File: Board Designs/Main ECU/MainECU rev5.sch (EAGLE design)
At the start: 164 parts, among them Q10 MMBT3904LT3G, Q11 MMBT3904LT3G, Q9 MMBT3904LT3G, X1 CONNECTOR-37, X2 CONNECTOR-4AUTOSPORT, X3 CONNECTOR-4NANO-FIT-VERTICAL-4, X4 CONNECTOR-4NANO-FIT-VERTICAL-4

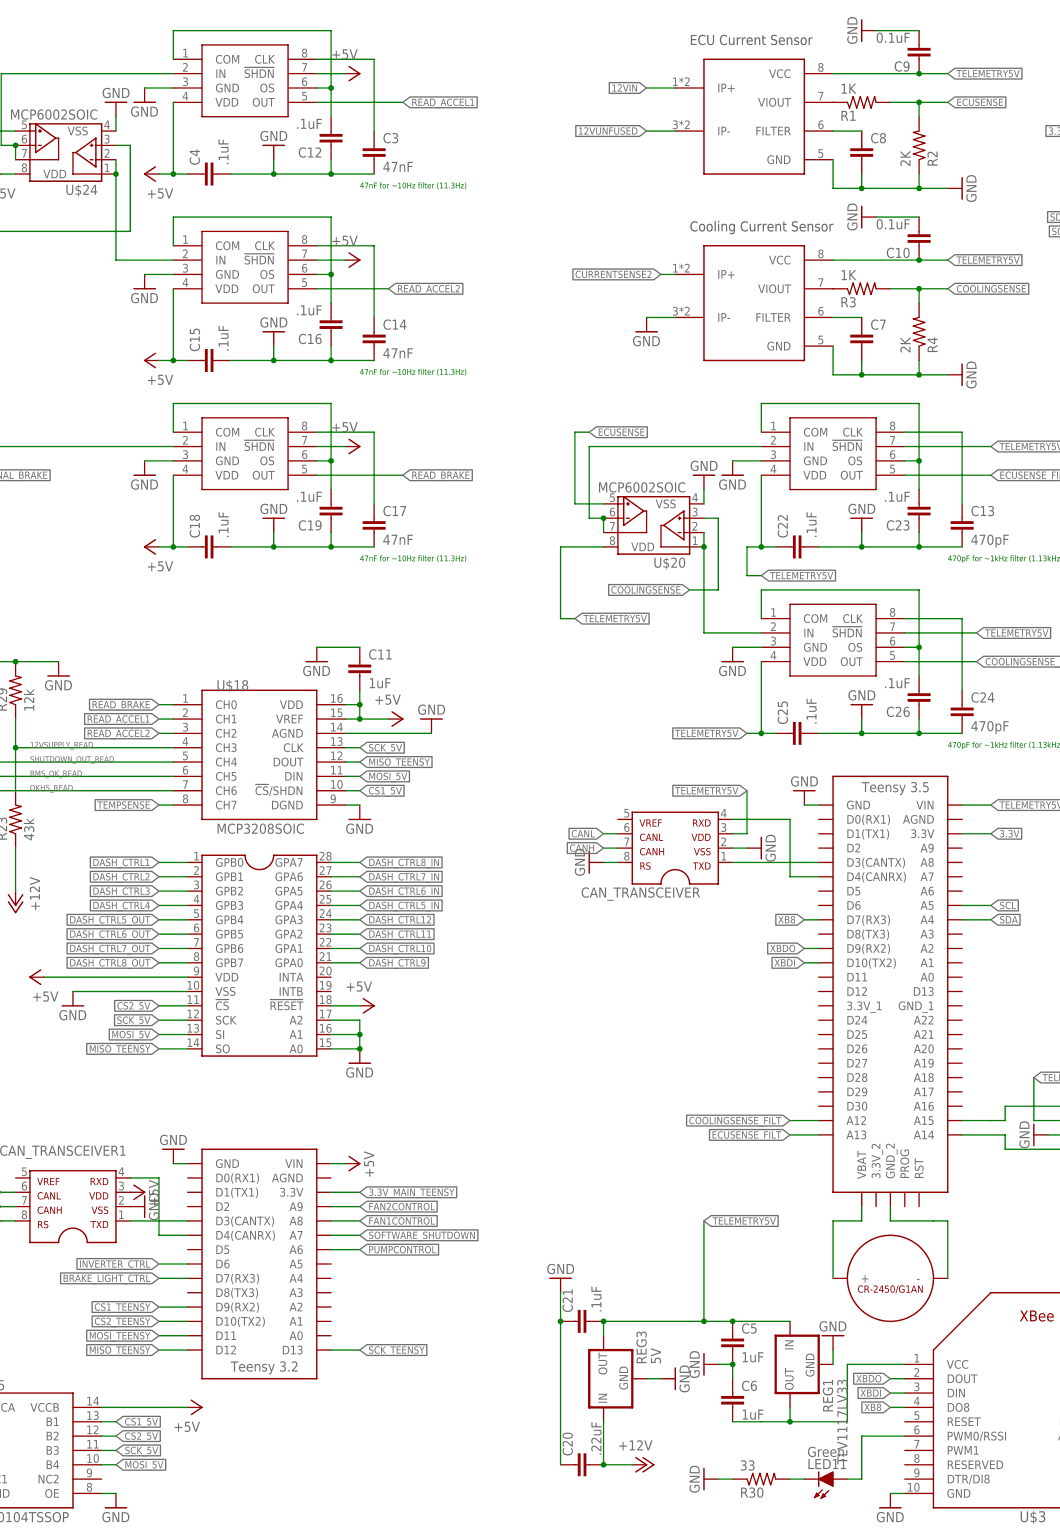
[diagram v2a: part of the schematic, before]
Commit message: MainECU rev5: Added current sensor filter caps, fixed level shifter OE pin, various tweaks to traces
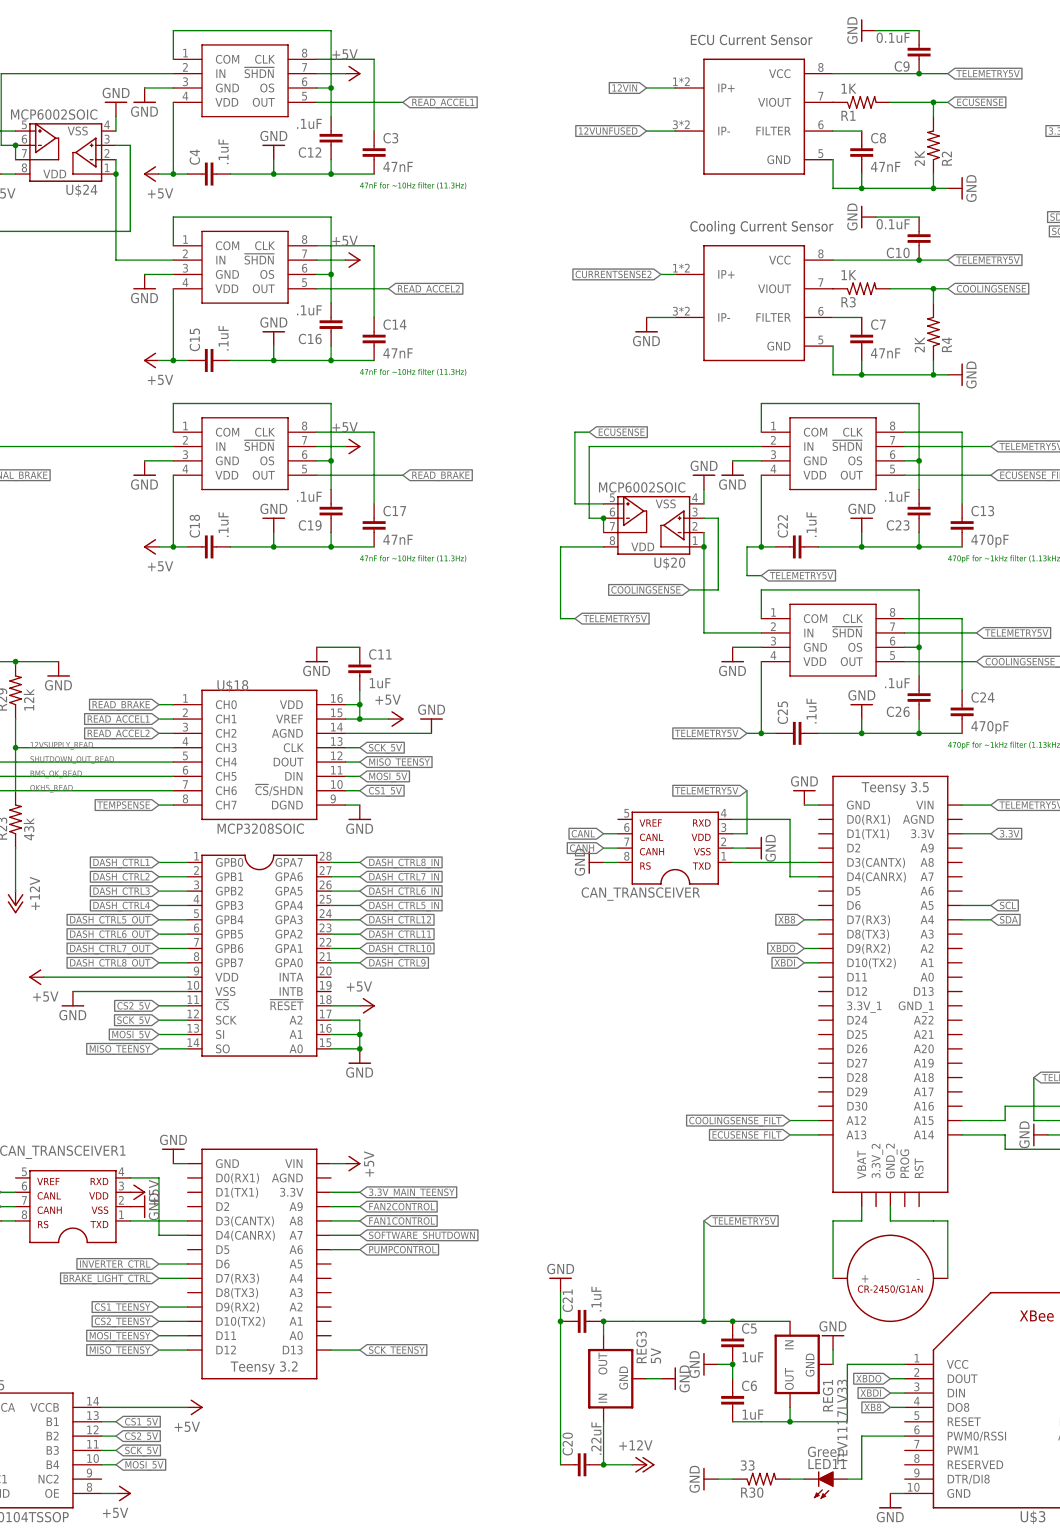
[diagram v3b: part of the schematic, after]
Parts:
- C7, C8: value (none) -> 47nF
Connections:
- net +5V: now also U$25.OE
- net GND: no longer U$25.OE
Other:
- moved on the sheet: R2, R4
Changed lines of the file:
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@@
 <part name="GND25" library="HyTechSymbols" deviceset="GND" device=""/>
 <part name="GND41" library="HyTechSymbols" deviceset="GND" device=""/>
-<part name="C7" library="HyTechDevices" deviceset="CAP" device="0805"/>
-<part name="C8" library="HyTechDevices" deviceset="CAP" device="0805"/>
+<part name="C7" library="HyTechDevices" deviceset="CAP" device="0805" value="47nF"/>
+<part name="C8" library="HyTechDevices" deviceset="CAP" device="0805" value="47nF"/>
 <part name="C9" library="HyTechDevices" deviceset="CAP" device="0805" value="0.1uF"/>
 <part name="C10" library="HyTechDevices" deviceset="CAP" device="0805" value="0.1uF"/>
@@
 <part name="R50" library="HyTechDevices" deviceset="RESISTOR" device="0805-RES" value="1k"/>
 <part name="FLIP" library="supply1" library_urn="urn:adsk.eagle:library:371" deviceset="+5V" device=""/>
-<part name="GND42" library="HyTechSymbols" deviceset="GND" device=""/>
 <part name="GND43" library="HyTechSymbols" deviceset="GND" device=""/>
 <part name="U$25" library="HyTechDevices" deviceset="TXB0104" device="TSSOP"/>
@@
 <part name="R52" library="HyTechDevices" deviceset="RESISTOR" device="0805-RES" value="100"/>
 <part name="GND79" library="HyTechSymbols" deviceset="GND" device=""/>
+<part name="FLIP1" library="supply1" library_urn="urn:adsk.eagle:library:371" deviceset="+5V" device=""/>
 </parts>
 <sheets>
@@
 <attribute name="VALUE" x="443.23" y="257.302" size="1.778" layer="96" rot="MR180"/>
 </instance>
-<instance part="R2" gate="G$1" x="457.2" y="246.38" smashed="yes" rot="MR90">
-<attribute name="NAME" x="458.6986" y="242.57" size="1.778" layer="95" rot="MR90"/>
-<attribute name="VALUE" x="453.898" y="242.57" size="1.778" layer="96" rot="MR90"/>
+<instance part="R2" gate="G$1" x="459.74" y="246.38" smashed="yes" rot="MR90">
+<attribute name="NAME" x="461.2386" y="242.57" size="1.778" layer="95" rot="MR90"/>
+<attribute name="VALUE" x="456.438" y="242.57" size="1.778" layer="96" rot="MR90"/>
 </instance>
 <instance part="R3" gate="G$1" x="447.04" y="220.98" smashed="yes" rot="MR180">
@@
 <attribute name="VALUE" x="443.23" y="224.282" size="1.778" layer="96" rot="MR180"/>
 </instance>
-<instance part="R4" gate="G$1" x="457.2" y="213.36" smashed="yes" rot="MR90">
-<attribute name="NAME" x="458.6986" y="209.55" size="1.778" layer="95" rot="MR90"/>
-<attribute name="VALUE" x="453.898" y="209.55" size="1.778" layer="96" rot="MR90"/>
+<instance part="R4" gate="G$1" x="459.74" y="213.36" smashed="yes" rot="MR90">
+<attribute name="NAME" x="461.2386" y="209.55" size="1.778" layer="95" rot="MR90"/>
+<attribute name="VALUE" x="456.438" y="209.55" size="1.778" layer="96" rot="MR90"/>
 </instance>
 <instance part="CAN_TRANSCEIVER" gate="G$1" x="421.64" y="127" smashed="yes" rot="R180">
@@
 <attribute name="VALUE" x="325.12" y="20.32" size="1.778" layer="96" rot="MR180"/>
 </instance>
-<instance part="GND42" gate="1" x="314.96" y="5.08" smashed="yes">
-<attribute name="VALUE" x="312.42" y="2.54" size="1.778" layer="96"/>
-</instance>
 <instance part="GND43" gate="1" x="281.94" y="5.08" smashed="yes">
 <attribute name="VALUE" x="279.4" y="2.54" size="1.778" layer="96"/>
@@
 <instance part="GND79" gate="1" x="584.2" y="137.16" smashed="yes">
 <attribute name="VALUE" x="581.66" y="134.62" size="1.778" layer="96"/>
+</instance>
+<instance part="FLIP1" gate="1" x="317.5" y="7.62" smashed="yes" rot="MR90">
+<attribute name="VALUE" x="312.42" y="5.08" size="1.778" layer="96" rot="MR180"/>
 </instance>
 </instances>
@@
 <segment>
 <pinref part="GND25" gate="1" pin="GND"/>
-<wire x1="462.28" y1="205.74" x2="457.2" y2="205.74" width="0.1524" layer="91"/>
+<wire x1="462.28" y1="205.74" x2="459.74" y2="205.74" width="0.1524" layer="91"/>
 <pinref part="U$10" gate="G$1" pin="GND"/>
-<wire x1="457.2" y1="205.74" x2="447.04" y2="205.74" width="0.1524" layer="91"/>
+<wire x1="459.74" y1="205.74" x2="447.04" y2="205.74" width="0.1524" layer="91"/>
 <wire x1="447.04" y1="205.74" x2="441.96" y2="205.74" width="0.1524" layer="91"/>
 <wire x1="441.96" y1="205.74" x2="441.96" y2="210.82" width="0.1524" layer="91"/>
@@
 <junction x="447.04" y="205.74"/>
 <pinref part="R4" gate="G$1" pin="1"/>
-<wire x1="457.2" y1="208.28" x2="457.2" y2="205.74" width="0.1524" layer="91"/>
-<junction x="457.2" y="205.74"/>
+<wire x1="459.74" y1="208.28" x2="459.74" y2="205.74" width="0.1524" layer="91"/>
+<junction x="459.74" y="205.74"/>
 </segment>
 <segment>
@@
 <segment>
 <pinref part="GND41" gate="1" pin="GND"/>
-<wire x1="462.28" y1="238.76" x2="457.2" y2="238.76" width="0.1524" layer="91"/>
+<wire x1="462.28" y1="238.76" x2="459.74" y2="238.76" width="0.1524" layer="91"/>
 <pinref part="U$9" gate="G$1" pin="GND"/>
-<wire x1="457.2" y1="238.76" x2="447.04" y2="238.76" width="0.1524" layer="91"/>
+<wire x1="459.74" y1="238.76" x2="447.04" y2="238.76" width="0.1524" layer="91"/>
 <wire x1="447.04" y1="238.76" x2="441.96" y2="238.76" width="0.1524" layer="91"/>
 <wire x1="441.96" y1="238.76" x2="441.96" y2="243.84" width="0.1524" layer="91"/>
@@
 <junction x="447.04" y="238.76"/>
 <pinref part="R2" gate="G$1" pin="1"/>
-<wire x1="457.2" y1="241.3" x2="457.2" y2="238.76" width="0.1524" layer="91"/>
-<junction x="457.2" y="238.76"/>
+<wire x1="459.74" y1="241.3" x2="459.74" y2="238.76" width="0.1524" layer="91"/>
+<junction x="459.74" y="238.76"/>
 </segment>
 <segment>
@@
 <pinref part="GND11" gate="1" pin="GND"/>
 <wire x1="203.2" y1="195.58" x2="203.2" y2="193.04" width="0.1524" layer="91"/>
-</segment>
-<segment>
-<wire x1="312.42" y1="7.62" x2="314.96" y2="7.62" width="0.1524" layer="91"/>
-<pinref part="GND42" gate="1" pin="GND"/>
-<pinref part="U$25" gate="G$1" pin="OE"/>
 </segment>
 <segment>
@@
 <pinref part="U$25" gate="G$1" pin="VCCB"/>
 </segment>
+<segment>
+<wire x1="312.42" y1="7.62" x2="314.96" y2="7.62" width="0.1524" layer="91"/>
+<pinref part="U$25" gate="G$1" pin="OE"/>
+<pinref part="FLIP1" gate="1" pin="+5V"/>
+</segment>
 </net>
 <net name="IMD_PWR_STEP" class="0">
@@
 <pinref part="R1" gate="G$1" pin="2"/>
 <pinref part="R2" gate="G$1" pin="2"/>
-<wire x1="452.12" y1="254" x2="457.2" y2="254" width="0.1524" layer="91"/>
+<wire x1="452.12" y1="254" x2="459.74" y2="254" width="0.1524" layer="91"/>
 <label x="462.28" y="254" size="1.27" layer="95" xref="yes"/>
-<wire x1="457.2" y1="254" x2="462.28" y2="254" width="0.1524" layer="91"/>
-<wire x1="457.2" y1="251.46" x2="457.2" y2="254" width="0.1524" layer="91"/>
-<junction x="457.2" y="254"/>
+<wire x1="459.74" y1="254" x2="462.28" y2="254" width="0.1524" layer="91"/>
+<wire x1="459.74" y1="251.46" x2="459.74" y2="254" width="0.1524" layer="91"/>
+<junction x="459.74" y="254"/>
 </segment>
 <segment>
@@
 <pinref part="R3" gate="G$1" pin="2"/>
 <pinref part="R4" gate="G$1" pin="2"/>
-<wire x1="452.12" y1="220.98" x2="457.2" y2="220.98" width="0.1524" layer="91"/>
-<wire x1="457.2" y1="220.98" x2="457.2" y2="218.44" width="0.1524" layer="91"/>
-<wire x1="457.2" y1="220.98" x2="462.28" y2="220.98" width="0.1524" layer="91"/>
-<junction x="457.2" y="220.98"/>
+<wire x1="452.12" y1="220.98" x2="459.74" y2="220.98" width="0.1524" layer="91"/>
+<wire x1="459.74" y1="220.98" x2="459.74" y2="218.44" width="0.1524" layer="91"/>
+<wire x1="459.74" y1="220.98" x2="462.28" y2="220.98" width="0.1524" layer="91"/>
+<junction x="459.74" y="220.98"/>
 <label x="462.28" y="220.98" size="1.27" layer="95" xref="yes"/>
 </segment>

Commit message: Main ECU rev{1-5}: Update values of LED resistors based on testing
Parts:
- LED7: value Green -> 20k
- R11: value 43 -> 150
- R14, R21: value 820 -> 2k
- R16, R25, R32, R51, R52: value 100 -> 1.2k
- R31: value 1.2K -> 6.8k
- R45: value 33 -> 0
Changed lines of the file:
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@@
 <part name="BMS_SSR" library="HyTechDevices" deviceset="CPC1002N" device=""/>
 <part name="GND3" library="HyTechSymbols" deviceset="GND" device=""/>
-<part name="R11" library="HyTechDevices" deviceset="RESISTOR" device="0805-RES" value="43"/>
+<part name="R11" library="HyTechDevices" deviceset="RESISTOR" device="0805-RES" value="150"/>
 <part name="R12" library="HyTechDevices" deviceset="RESISTOR" device="0805-RES" value="33"/>
 <part name="BMS_LATCH_SSR" library="HyTechDevices" deviceset="CPC1002N" device=""/>
@@
 <part name="LED3" library="HyTechDevices" deviceset="LED" device="-0805" value="Green"/>
 <part name="LED5" library="HyTechDevices" deviceset="LED" device="-0805" value="Yellow"/>
-<part name="R14" library="HyTechDevices" deviceset="RESISTOR" device="0805-RES" value="820"/>
+<part name="R14" library="HyTechDevices" deviceset="RESISTOR" device="0805-RES" value="2k"/>
 <part name="GND6" library="HyTechSymbols" deviceset="GND" device=""/>
 <part name="IMD_SHUTDOWN1" library="HyTechDevices" deviceset="G2RL-2-DC12" device=""/>
 <part name="GND19" library="HyTechSymbols" deviceset="GND" device=""/>
 <part name="R17" library="HyTechDevices" deviceset="RESISTOR" device="0805-RES" value="820"/>
-<part name="LED7" library="HyTechDevices" deviceset="LED" device="-0805" value="Green"/>
+<part name="LED7" library="HyTechDevices" deviceset="LED" device="-0805" value="20k"/>
 <part name="GND20" library="HyTechSymbols" deviceset="GND" device=""/>
 <part name="GND21" library="HyTechSymbols" deviceset="GND" device=""/>
@@
 <part name="LED9" library="HyTechDevices" deviceset="LED" device="-0805" value="Yellow"/>
 <part name="GND24" library="HyTechSymbols" deviceset="GND" device=""/>
-<part name="R21" library="HyTechDevices" deviceset="RESISTOR" device="0805-RES" value="820"/>
+<part name="R21" library="HyTechDevices" deviceset="RESISTOR" device="0805-RES" value="2k"/>
 <part name="P+10" library="supply1" deviceset="+12V" device=""/>
 <part name="P+5" library="supply1" deviceset="+12V" device=""/>
@@
 <part name="LED18" library="HyTechDevices" deviceset="LED" device="-0805" value="RED"/>
 <part name="GND45" library="HyTechSymbols" deviceset="GND" device=""/>
-<part name="R31" library="HyTechDevices" deviceset="RESISTOR" device="0805-RES" value="1.2K"/>
+<part name="R31" library="HyTechDevices" deviceset="RESISTOR" device="0805-RES" value="6.8k"/>
 <part name="GND1" library="HyTechSymbols" deviceset="GND" device=""/>
 <part name="GND4" library="HyTechSymbols" deviceset="GND" device=""/>
@@
 <part name="GND53" library="HyTechSymbols" deviceset="GND" device=""/>
 <part name="LED10" library="HyTechDevices" deviceset="LED" device="-0805" value="Red"/>
-<part name="R32" library="HyTechDevices" deviceset="RESISTOR" device="0805-RES" value="100"/>
+<part name="R32" library="HyTechDevices" deviceset="RESISTOR" device="0805-RES" value="1.2k"/>
 <part name="GND54" library="HyTechSymbols" deviceset="GND" device=""/>
 <part name="R33" library="HyTechDevices" deviceset="RESISTOR" device="0805-RES" value="4.7k"/>
@@
 <part name="P+35" library="supply1" library_urn="urn:adsk.eagle:library:371" deviceset="+5V" device=""/>
 <part name="LED14" library="HyTechDevices" deviceset="LED" device="-0805" value="Blue"/>
-<part name="R45" library="HyTechDevices" deviceset="RESISTOR" device="0805-RES" value="33"/>
+<part name="R45" library="HyTechDevices" deviceset="RESISTOR" device="0805-RES" value="0"/>
 <part name="GND62" library="HyTechSymbols" deviceset="GND" device=""/>
 <part name="X3" library="HyTechDevices" deviceset="CONNECTOR-4" device="NANO-FIT-VERTICAL-4"/>
@@
 <part name="LED6" library="HyTechDevices" deviceset="LED" device="-0805" value="Red"/>
 <part name="GND17" library="HyTechSymbols" deviceset="GND" device=""/>
-<part name="R16" library="HyTechDevices" deviceset="RESISTOR" device="0805-RES" value="100"/>
+<part name="R16" library="HyTechDevices" deviceset="RESISTOR" device="0805-RES" value="1.2k"/>
 <part name="P+8" library="supply1" deviceset="+12V" device=""/>
 <part name="P+12" library="supply1" deviceset="+12V" device=""/>
@@
 <part name="P+36" library="supply1" deviceset="+12V" device=""/>
 <part name="LED4" library="HyTechDevices" deviceset="LED" device="-0805" value="Red"/>
-<part name="R25" library="HyTechDevices" deviceset="RESISTOR" device="0805-RES" value="100"/>
+<part name="R25" library="HyTechDevices" deviceset="RESISTOR" device="0805-RES" value="1.2k"/>
 <part name="GND77" library="HyTechSymbols" deviceset="GND" device=""/>
 <part name="LED12" library="HyTechDevices" deviceset="LED" device="-0805" value="Red"/>
-<part name="R51" library="HyTechDevices" deviceset="RESISTOR" device="0805-RES" value="100"/>
+<part name="R51" library="HyTechDevices" deviceset="RESISTOR" device="0805-RES" value="1.2k"/>
 <part name="GND78" library="HyTechSymbols" deviceset="GND" device=""/>
 <part name="LED13" library="HyTechDevices" deviceset="LED" device="-0805" value="Red"/>
-<part name="R52" library="HyTechDevices" deviceset="RESISTOR" device="0805-RES" value="100"/>
+<part name="R52" library="HyTechDevices" deviceset="RESISTOR" device="0805-RES" value="1.2k"/>
 <part name="GND79" library="HyTechSymbols" deviceset="GND" device=""/>
 <part name="FLIP1" library="supply1" library_urn="urn:adsk.eagle:library:371" deviceset="+5V" device=""/>
